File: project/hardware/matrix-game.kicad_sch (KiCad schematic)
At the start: 31 parts, among them SW1 button_center, SW2 button_left, SW3 button_down, SW4 button_right, SW5 button_up, U1 NUCLEO-F042K6, U2 MAX7219, U3 DM-OLED096-636

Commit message: [project/hardware] changed value of R1
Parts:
- R1: value 10k -> 22k
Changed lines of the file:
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@@
 			)
 		)
-		(property "Value" "10k"
-			(at 175.26 44.4499 0)
+		(property "Value" "22k"
+			(at 172.72 27.9401 0)
 			(effects
 				(font

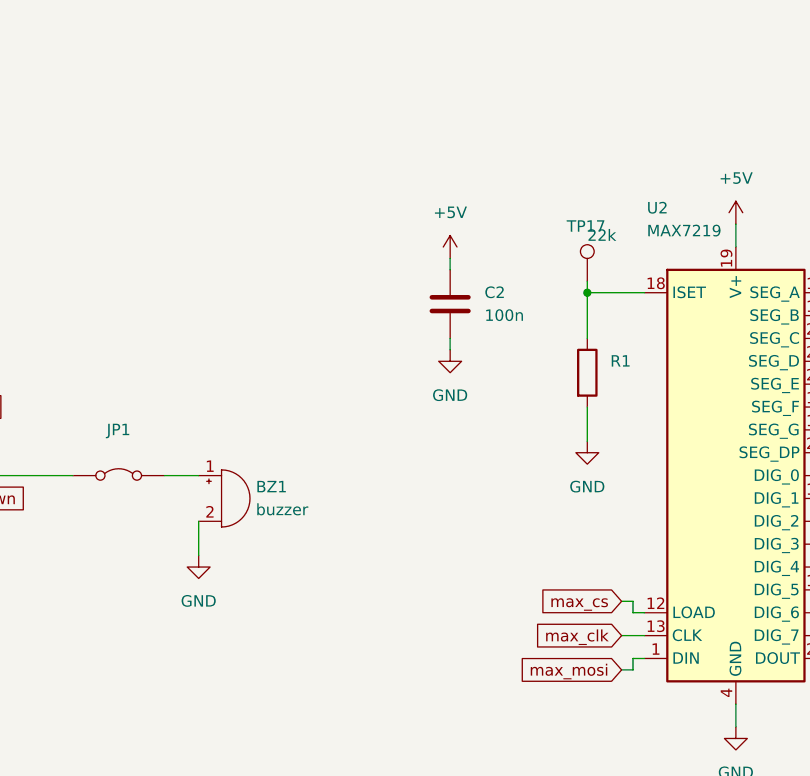
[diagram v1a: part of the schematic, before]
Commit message: [project/hardware] fix: wrong connection of R1
R1 was wrongly connectet to GND instead of +5V
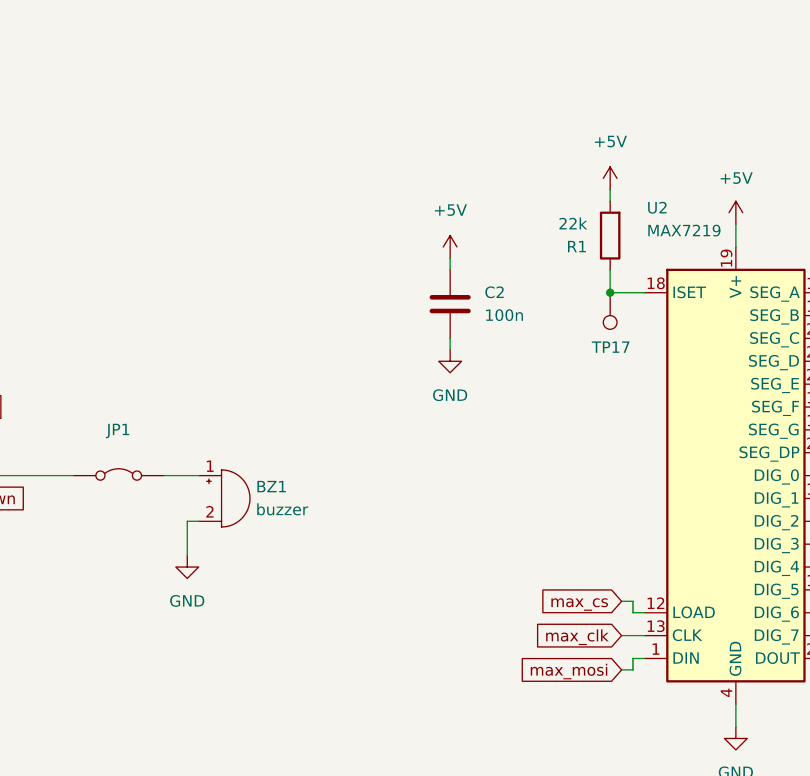
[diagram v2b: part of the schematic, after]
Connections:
- net +5V: now also R1.2
- net GND: no longer R1.2
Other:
- moved on the sheet: R1, TP17

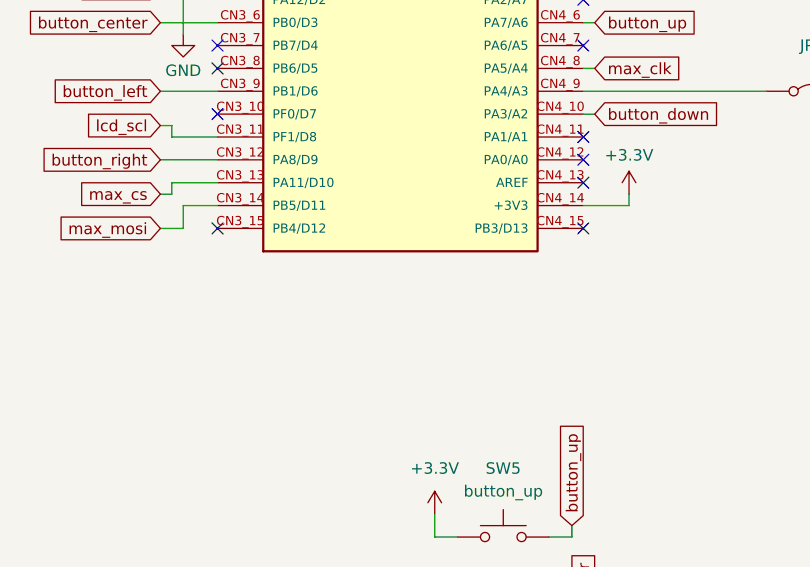
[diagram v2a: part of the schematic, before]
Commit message: [project/hardware] added text: Remove JP on Nucleo between D2 and GND!
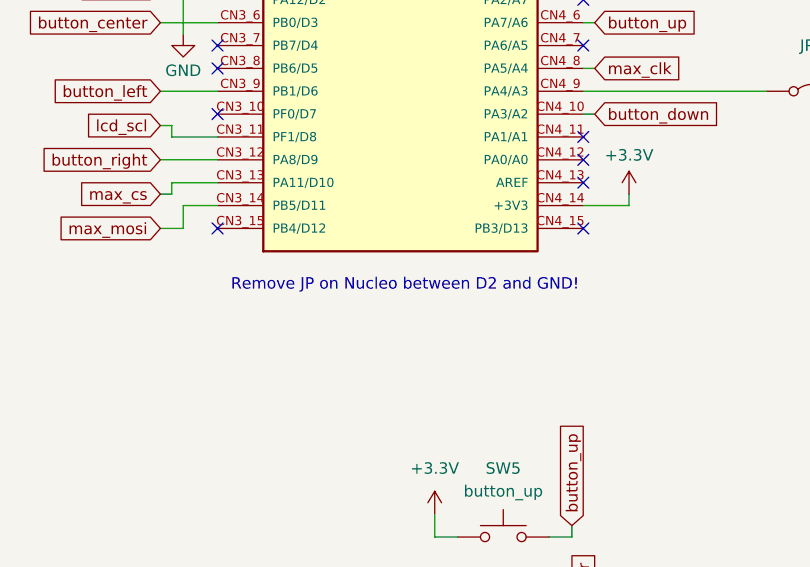
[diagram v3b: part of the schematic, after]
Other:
- note added: "Remove JP on Nucleo between D2 and GND!"
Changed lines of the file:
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@@
+		)
+	)
+	(text "Remove JP on Nucleo between D2 and GND!"
+		(exclude_from_sim no)
+		(at 75.438 76.2 0)
+		(effects
+			(font
+				(size 1.27 1.27)
+			)
 		)
 	)
